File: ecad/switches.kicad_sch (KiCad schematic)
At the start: 40 parts, among them SW1 Kailh choc v2, SW12 Kailh choc v2, SW13 Kailh choc v2, SW14 Kailh choc v2, SW16 Kailh choc v2, SW17 Kailh choc v2, SW18 Kailh choc v2, SW19 Kailh choc v2, SW2 Kailh choc v2, SW20 Kailh choc v2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

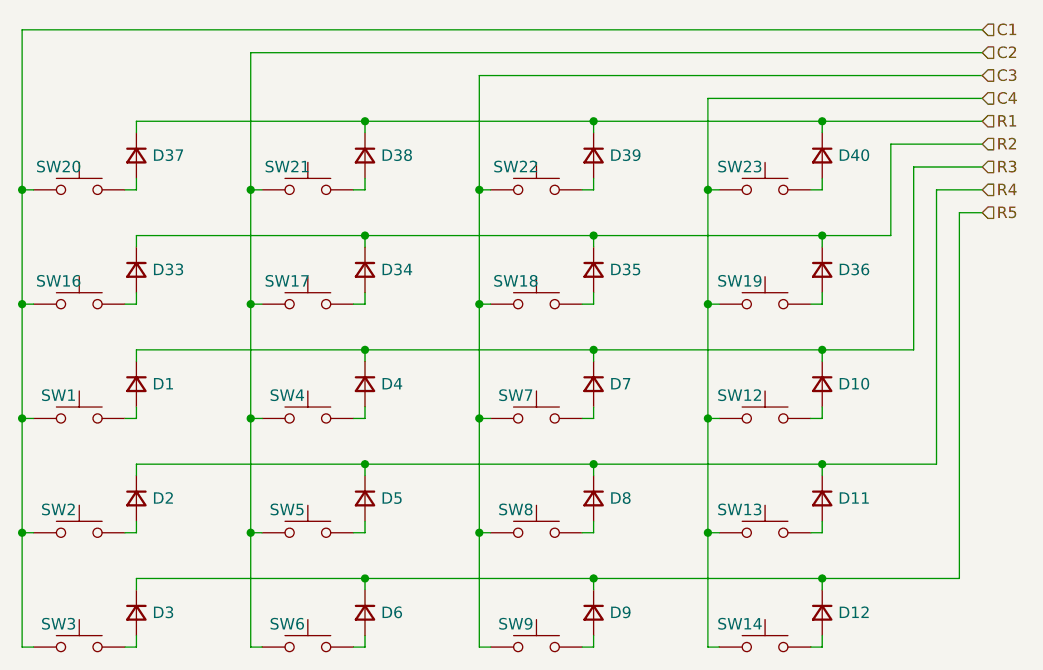
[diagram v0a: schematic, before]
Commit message: feat(ecad): change ref of swtiche diode and make the circuitry for the display
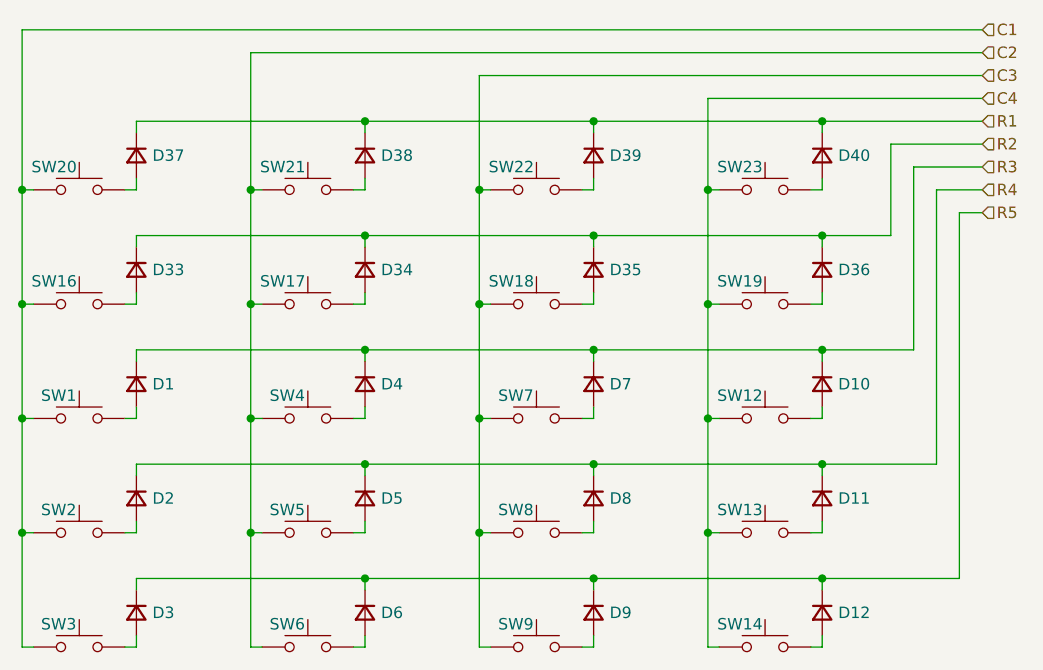
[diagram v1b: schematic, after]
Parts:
- D1, D10, D11, D12, D2, D3, D33, D34, D35, D36, D37, D38, D39, D4, D40, D5, D6, D7, D8, D9: value D_Small -> 1N4148W; footprint Diode_SMD:D_0402_1005Metric -> Diode_SMD:D_SOD-123
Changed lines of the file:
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@@
 		(dnp no)
 		(property "Reference" "SW21"
-			(at 115.824 80.01 0)
+			(at 115.316 80.01 0)
 			(effects
 				(font
@@
 			)
 		)
-		(property "Value" "D_Small"
+		(property "Value" "1N4148W"
 			(at 152.4 92.7099 90)
 			(effects
@@
 			)
 		)
-		(property "Footprint" "Diode_SMD:D_0402_1005Metric"
+		(property "Footprint" "Diode_SMD:D_SOD-123"
 			(at 149.86 91.44 90)
 			(effects
@@
 			)
 		)
-		(property "Value" "D_Small"
+		(property "Value" "1N4148W"
 			(at 101.6 92.7099 90)
 			(effects
@@
 			)
 		)
-		(property "Footprint" "Diode_SMD:D_0402_1005Metric"
+		(property "Footprint" "Diode_SMD:D_SOD-123"
 			(at 99.06 91.44 90)
 			(effects
@@
 			)
 		)
-		(property "Value" "D_Small"
+		(property "Value" "1N4148W"
 			(at 177.8 80.0099 90)
 			(effects
@@
 			)
 		)
-		(property "Footprint" "Diode_SMD:D_0402_1005Metric"
+		(property "Footprint" "Diode_SMD:D_SOD-123"
 			(at 175.26 78.74 90)
 			(effects
@@
 		(dnp no)
 		(property "Reference" "SW18"
-			(at 141.224 92.71 0)
+			(at 140.716 92.71 0)
 			(effects
 				(font
@@
 			)
 		)
-		(property "Value" "D_Small"
+		(property "Value" "1N4148W"
 			(at 152.4 80.0099 90)
 			(effects
@@
 			)
 		)
-		(property "Footprint" "Diode_SMD:D_0402_1005Metric"
+		(property "Footprint" "Diode_SMD:D_SOD-123"
 			(at 149.86 78.74 90)
 			(effects
@@
 		(dnp no)
 		(property "Reference" "SW17"
-			(at 115.824 92.71 0)
+			(at 115.316 92.71 0)
 			(effects
 				(font
@@
 			)
 		)
-		(property "Value" "D_Small"
+		(property "Value" "1N4148W"
 			(at 101.6 80.0099 90)
 			(effects
@@
 			)
 		)
-		(property "Footprint" "Diode_SMD:D_0402_1005Metric"
+		(property "Footprint" "Diode_SMD:D_SOD-123"
 			(at 99.06 78.74 90)
 			(effects
@@
 			)
 		)
-		(property "Value" "D_Small"
+		(property "Value" "1N4148W"
 			(at 101.6 130.8099 90)
 			(effects
@@
 			)
 		)
-		(property "Footprint" "Diode_SMD:D_0402_1005Metric"
+		(property "Footprint" "Diode_SMD:D_SOD-123"
 			(at 99.06 129.54 90)
 			(effects
@@
 			)
 		)
-		(property "Value" "D_Small"
+		(property "Value" "1N4148W"
 			(at 101.6 118.1099 90)
 			(effects
@@
 			)
 		)
-		(property "Footprint" "Diode_SMD:D_0402_1005Metric"
+		(property "Footprint" "Diode_SMD:D_SOD-123"
 			(at 99.06 116.84 90)
 			(effects
@@
 			)
 		)
-		(property "Value" "D_Small"
+		(property "Value" "1N4148W"
 			(at 177.8 130.8099 90)
 			(effects
@@
 			)
 		)
-		(property "Footprint" "Diode_SMD:D_0402_1005Metric"
+		(property "Footprint" "Diode_SMD:D_SOD-123"
 			(at 175.26 129.54 90)
 			(effects
@@
 			)
 		)
-		(property "Value" "D_Small"
+		(property "Value" "1N4148W"
 			(at 127 80.0099 90)
 			(effects
@@
 			)
 		)
-		(property "Footprint" "Diode_SMD:D_0402_1005Metric"
+		(property "Footprint" "Diode_SMD:D_SOD-123"
 			(at 124.46 78.74 90)
 			(effects
@@
 			)
 		)
-		(property "Value" "D_Small"
+		(property "Value" "1N4148W"
 			(at 127 105.4099 90)
 			(effects
@@
 			)
 		)
-		(property "Footprint" "Diode_SMD:D_0402_1005Metric"
+		(property "Footprint" "Diode_SMD:D_SOD-123"
 			(at 124.46 104.14 90)
 			(effects
@@
 			)
 		)
-		(property "Value" "D_Small"
+		(property "Value" "1N4148W"
 			(at 127 92.7099 90)
 			(effects
@@
 			)
 		)
-		(property "Footprint" "Diode_SMD:D_0402_1005Metric"
+		(property "Footprint" "Diode_SMD:D_SOD-123"
 			(at 124.46 91.44 90)
 			(effects
@@
 			)
 		)
-		(property "Value" "D_Small"
+		(property "Value" "1N4148W"
 			(at 152.4 130.8099 90)
 			(effects
@@
 			)
 		)
-		(property "Footprint" "Diode_SMD:D_0402_1005Metric"
+		(property "Footprint" "Diode_SMD:D_SOD-123"
 			(at 149.86 129.54 90)
 			(effects
@@
 			)
 		)
-		(property "Value" "D_Small"
+		(property "Value" "1N4148W"
 			(at 127 130.8099 90)
 			(effects
@@
 			)
 		)
-		(property "Footprint" "Diode_SMD:D_0402_1005Metric"
+		(property "Footprint" "Diode_SMD:D_SOD-123"
 			(at 124.46 129.54 90)
 			(effects
@@
 			)
 		)
-		(property "Value" "D_Small"
+		(property "Value" "1N4148W"
 			(at 177.8 105.4099 90)
 			(effects
@@
 			)
 		)
-		(property "Footprint" "Diode_SMD:D_0402_1005Metric"
+		(property "Footprint" "Diode_SMD:D_SOD-123"
 			(at 175.26 104.14 90)
 			(effects
@@
 			)
 		)
-		(property "Value" "D_Small"
+		(property "Value" "1N4148W"
 			(at 152.4 105.4099 90)
 			(effects
@@
 			)
 		)
-		(property "Footprint" "Diode_SMD:D_0402_1005Metric"
+		(property "Footprint" "Diode_SMD:D_SOD-123"
 			(at 149.86 104.14 90)
 			(effects
@@
 		(dnp no)
 		(property "Reference" "SW16"
-			(at 90.424 92.71 0)
+			(at 89.916 92.71 0)
 			(effects
 				(font
@@
 			)
 		)
-		(property "Value" "D_Small"
+		(property "Value" "1N4148W"
 			(at 101.6 105.4099 90)
 			(effects
@@
 			)
 		)
-		(property "Footprint" "Diode_SMD:D_0402_1005Metric"
+		(property "Footprint" "Diode_SMD:D_SOD-123"
 			(at 99.06 104.14 90)
 			(effects
@@
 		(dnp no)
 		(property "Reference" "SW20"
-			(at 90.424 80.01 0)
+			(at 89.916 80.01 0)
 			(effects
 				(font
@@
 		(dnp no)
 		(property "Reference" "SW22"
-			(at 141.224 80.01 0)
+			(at 140.716 80.01 0)
 			(effects
 				(font
@@
 			)
 		)
-		(property "Value" "D_Small"
+		(property "Value" "1N4148W"
 			(at 127 118.1099 90)
 			(effects
@@
 			)
 		)
-		(property "Footprint" "Diode_SMD:D_0402_1005Metric"
+		(property "Footprint" "Diode_SMD:D_SOD-123"
 			(at 124.46 116.84 90)
 			(effects
@@
 			)
 		)
-		(property "Value" "D_Small"
+		(property "Value" "1N4148W"
 			(at 152.4 118.1099 90)
 			(effects
@@
 			)
 		)
-		(property "Footprint" "Diode_SMD:D_0402_1005Metric"
+		(property "Footprint" "Diode_SMD:D_SOD-123"
 			(at 149.86 116.84 90)
 			(effects
@@
 			)
 		)
-		(property "Value" "D_Small"
+		(property "Value" "1N4148W"
 			(at 177.8 92.7099 90)
 			(effects
@@
 			)
 		)
-		(property "Footprint" "Diode_SMD:D_0402_1005Metric"
+		(property "Footprint" "Diode_SMD:D_SOD-123"
 			(at 175.26 91.44 90)
 			(effects
@@
 			)
 		)
-		(property "Value" "D_Small"
+		(property "Value" "1N4148W"
 			(at 177.8 118.1099 90)
 			(effects
@@
 			)
 		)
-		(property "Footprint" "Diode_SMD:D_0402_1005Metric"
+		(property "Footprint" "Diode_SMD:D_SOD-123"
 			(at 175.26 116.84 90)
 			(effects
